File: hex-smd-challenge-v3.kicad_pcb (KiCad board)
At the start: 2 copper layers, 44 x 50 mm, 29 parts, among them CON1 AVR-ISP-6, IC1 IC1, P0 CONN_01X01, P1 CONN_01X01, P2 CONN_01X01, P3 CONN_01X01, P4 CONN_01X01

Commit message: add new version of design including v2 which went to fab
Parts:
- CON1: moved to B.Cu
- moved CON1 0.32 mm to (222.8, 86.2)
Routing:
- net Net-(CON1-Pad5): track 0.00 -> 42.3 mm, vias 0 -> 1
- net Net-(CON1-Pad4): track 24.6 -> 41.6 mm, vias 0 -> 1
- net Net-(CON1-Pad1): track 15.1 -> 28.1 mm, vias 0 -> 1
- net +BATT: track 12.0 -> 24.7 mm, vias 2 -> 3
- net Net-(CON1-Pad3): track 27.0 -> 37.0 mm, vias 0 -> 1
- net GND: track 26.7 -> 16.9 mm, vias 2 -> 4
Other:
- board text added: "OSHPark.com/ SMDChallenge"
- board text removed: "OSHPark.com/SMDChallenge"

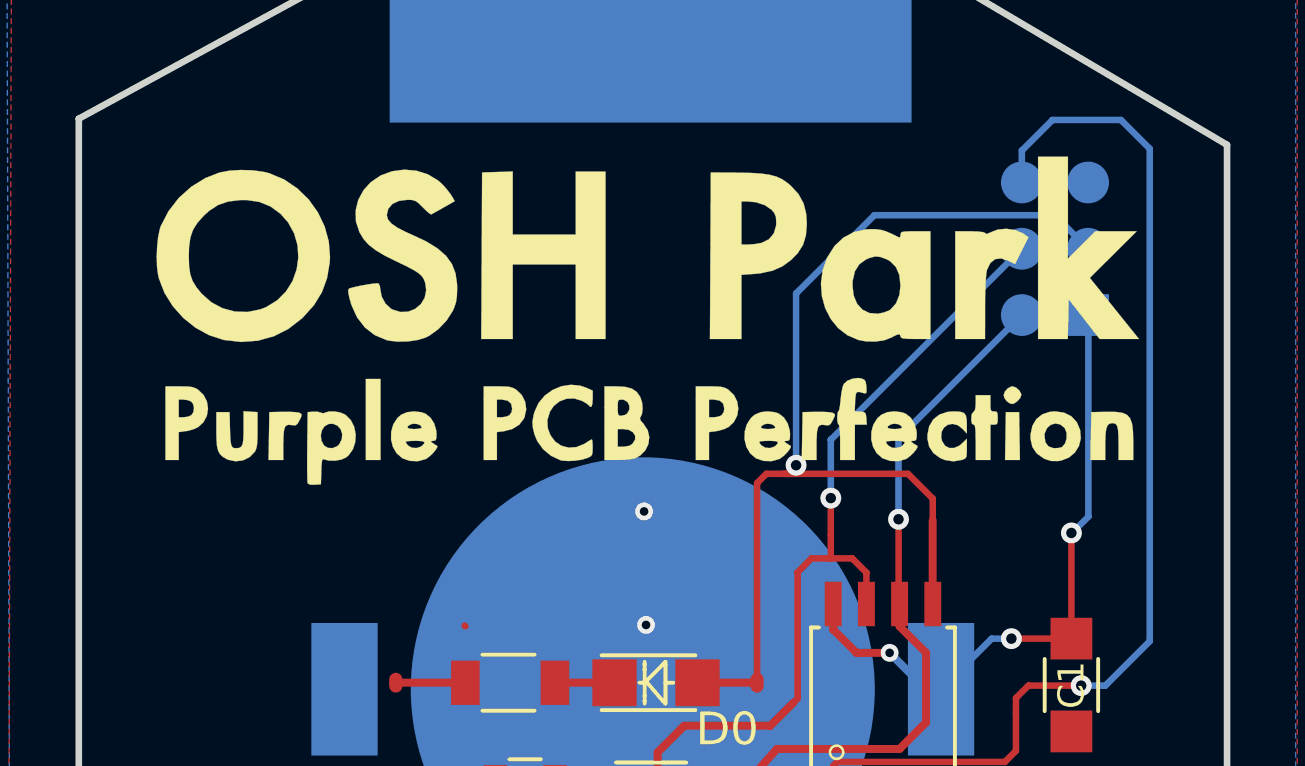
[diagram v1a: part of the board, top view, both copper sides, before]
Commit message: update logo based on svg
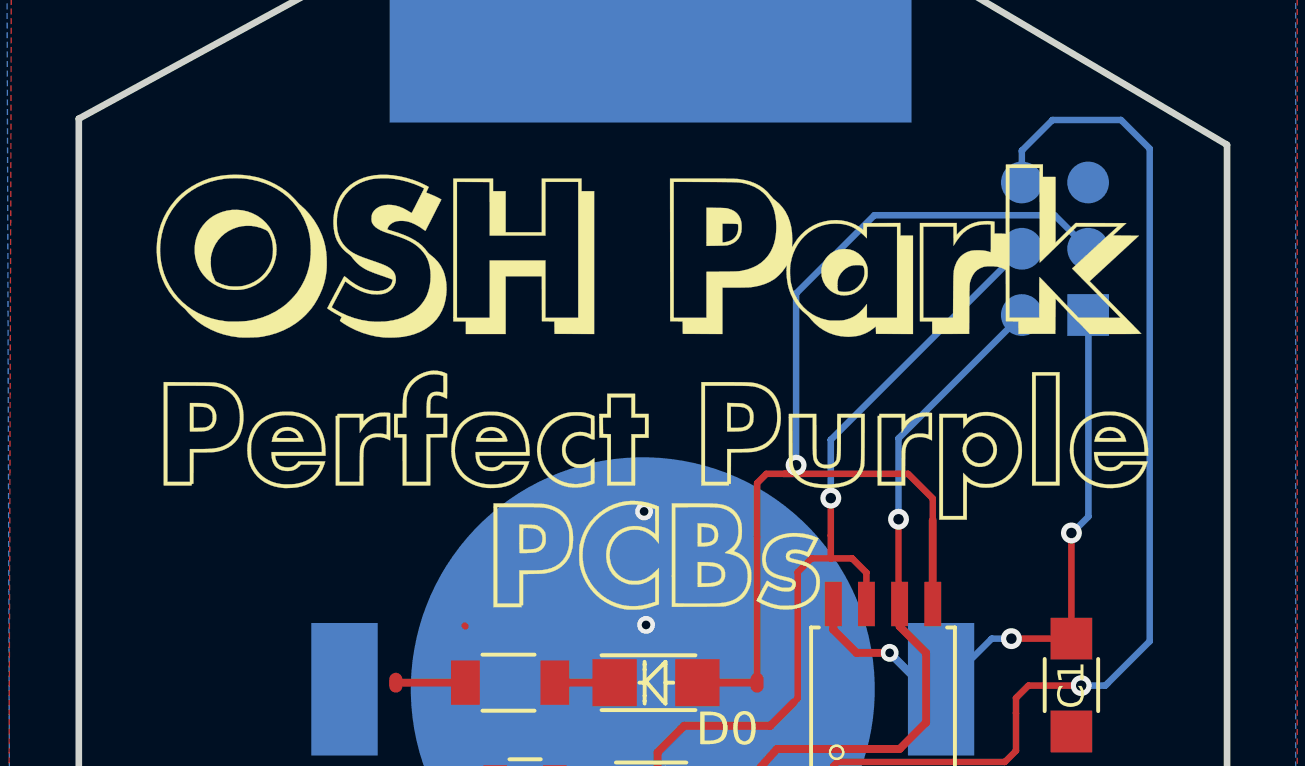
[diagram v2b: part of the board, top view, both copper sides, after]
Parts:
- removed G***: LOGO, myFootPrints:OSHParkPurple
- removed G***: LOGO, myFootPrints:OSHPark
- added Ref**: Val**, hex-smd-challenge:oshpark-v2-ppp, F.Cu at (212.9, 106.0)
- added Ref**: Val**, hex-smd-challenge:oshpark-v2-oshpark, F.Cu at (212.5, 107.1)

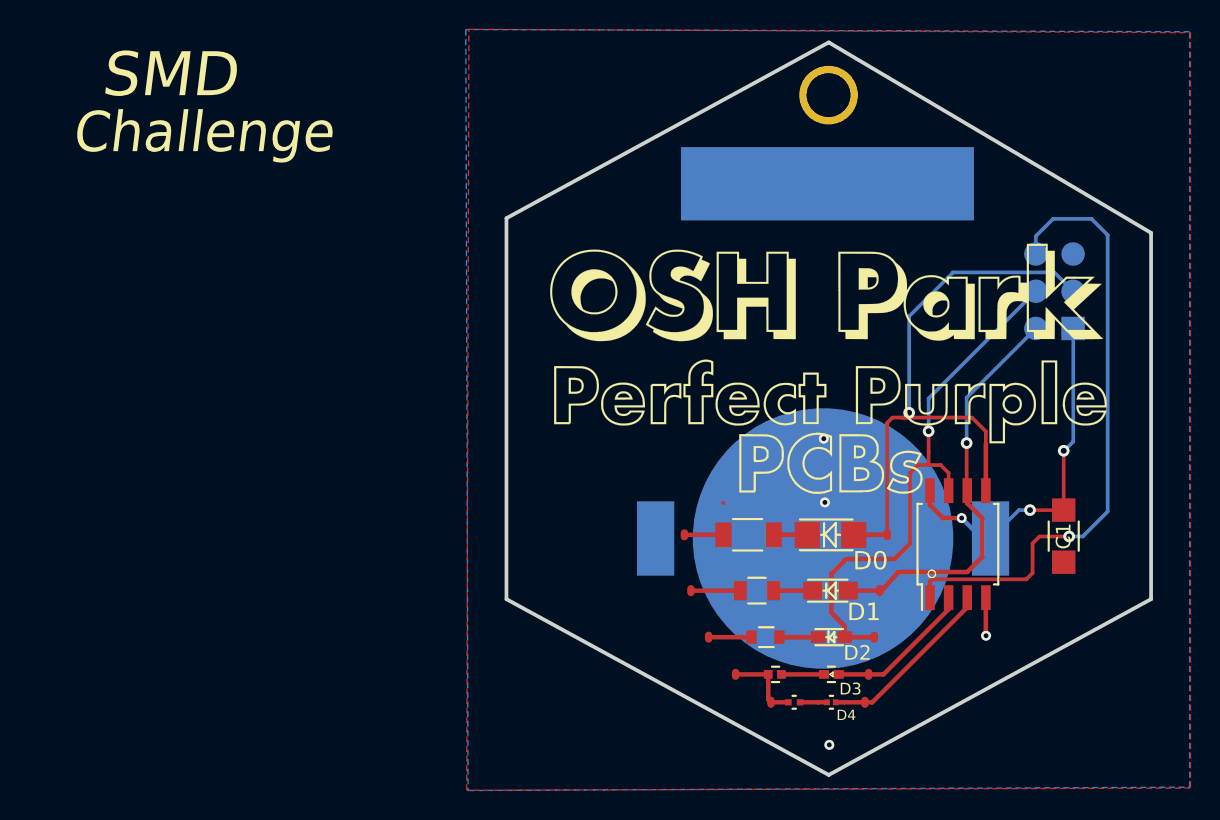
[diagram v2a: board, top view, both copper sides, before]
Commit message: improve oshpark text
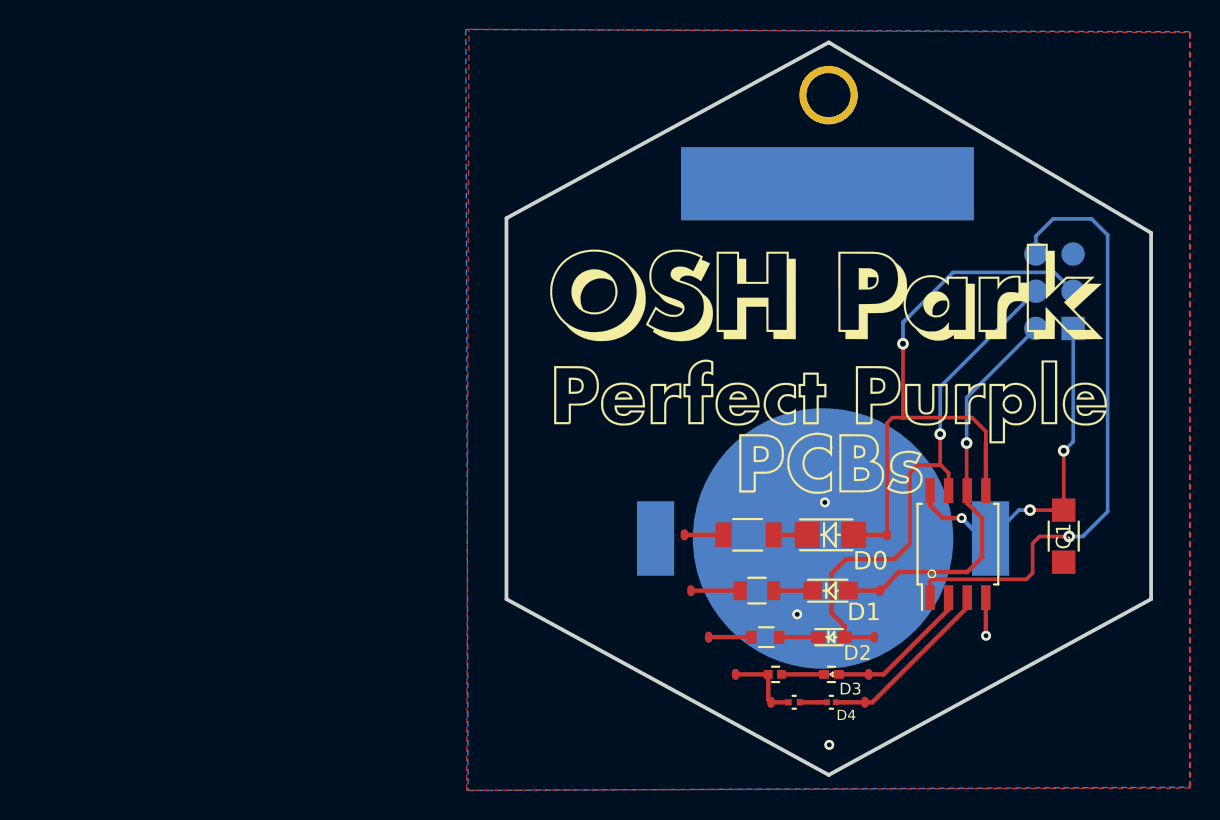
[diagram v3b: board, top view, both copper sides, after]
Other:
- board text removed: "Challenge"
- board text removed: "SMD"
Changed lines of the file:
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@@
     (effects (font (size 1 1) (thickness 0.15)) (justify left mirror))
-  )
-  (gr_text "SMD" (at 163.609 68.863) (layer "F.SilkS")
-    (effects (font (size 3 3) (thickness 0.75) italic))
-  )
-  (gr_text "Challenge" (at 165.895 72.8) (layer "F.SilkS")
-    (effects (font (size 2.75 2.6) (thickness 0.65) italic))
   )
   (segment (start 204.687 111.6925) (end 205.8745 111.6925) (width 0.3048) (layer "F.Cu") (net 1))
@@
   (segment (start 204.5045 109.7875) (end 204.5045 111.51) (width 0.3048) (layer "F.Cu") (net 1))
   (segment (start 202.274 109.7875) (end 204.5045 109.7875) (width 0.3048) (layer "F.Cu") (net 1))
-  (segment (start 201.4485 98.1035) (end 201.42 98.075) (width 0.25) (layer "F.Cu") (net 1))
   (segment (start 219.3555 107.1355) (end 219.37 107.15) (width 0.3048) (layer "F.Cu") (net 1))
   (segment (start 204.5045 111.51) (end 204.687 111.6925) (width 0.3048) (layer "F.Cu") (net 1))
   (segment (start 201.4485 100.2625) (end 198.7815 100.2625) (width 0.3048) (layer "F.Cu") (net 1))
   (segment (start 219.3555 104.5475) (end 219.3555 107.1355) (width 0.3048) (layer "F.Cu") (net 1))
-  (via (at 208.295 93.7) (size 0.6858) (drill 0.3302) (layers "F.Cu" "B.Cu") (net 1))
+  (via (at 206.48 105.69) (size 0.6858) (drill 0.3302) (layers "F.Cu" "B.Cu") (net 1))
   (via (at 208.67 114.6) (size 0.6858) (drill 0.3302) (layers "F.Cu" "B.Cu") (net 1))
   (via (at 219.37 107.15) (size 0.6858) (drill 0.3302) (layers "F.Cu" "B.Cu") (net 1))
@@
   (segment (start 222.77 86.175) (end 218.045 90.9) (width 0.25) (layer "B.Cu") (net 3))
   (segment (start 214.0215 101.0245) (end 213.1325 101.9135) (width 0.3048) (layer "F.Cu") (net 4))
+  (segment (start 216.24 93.39) (end 216.24 95.47) (width 0.25) (layer "F.Cu") (net 4))
+  (segment (start 216.24 95.47) (end 216.27 95.5) (width 0.25) (layer "F.Cu") (net 4))
   (segment (start 208.8145 102.9295) (end 209.7035 102.0405) (width 0.3048) (layer "F.Cu") (net 4))
   (segment (start 215.45 95.5) (end 216.27 95.5) (width 0.25) (layer "F.Cu") (net 4))
@@
   (segment (start 213.1325 101.9135) (end 209.8305 101.9135) (width 0.3048) (layer "F.Cu") (net 4))
   (segment (start 214.18 100.866) (end 214.18 96.03) (width 0.25) (layer "F.Cu") (net 4))
-  (segment (start 215.45 95.5) (end 215.45 94.62) (width 0.25) (layer "F.Cu") (net 4))
   (segment (start 214.0215 101.0245) (end 214.18 100.866) (width 0.25) (layer "F.Cu") (net 4))
   (segment (start 209.7035 106.4855) (end 208.8145 105.5965) (width 0.3048) (layer "F.Cu") (net 4))
   (segment (start 209.8305 101.9135) (end 209.7035 102.0405) (width 0.3048) (layer "F.Cu") (net 4))
-  (segment (start 215.45 94.62) (end 215.45 93.19) (width 0.25) (layer "F.Cu") (net 4))
   (segment (start 214.18 96.03) (end 214.71 95.5) (width 0.25) (layer "F.Cu") (net 4))
   (segment (start 208.8145 105.5965) (end 208.8145 102.9295) (width 0.3048) (layer "F.Cu") (net 4))
   (segment (start 216.27 95.5) (end 216.8155 96.0455) (width 0.25) (layer "F.Cu") (net 4))
   (segment (start 209.7035 107.2475) (end 211.7355 107.2475) (width 0.3048) (layer "F.Cu") (net 4))
-  (via (at 215.45 93.19) (size 0.8) (drill 0.4) (layers "F.Cu" "B.Cu") (net 4))
-  (segment (start 215.45 90.955) (end 215.45 93.19) (width 0.25) (layer "B.Cu") (net 4))
-  (segment (start 222.77 83.635) (end 215.4525 90.9525) (width 0.25) (layer "B.Cu") (net 4))
-  (segment (start 215.4525 90.9525) (end 215.45 90.955) (width 0.25) (layer "B.Cu") (net 4))
+  (via (at 216.24 93.39) (size 0.8) (drill 0.4) (layers "F.Cu" "B.Cu") (net 4))
+  (segment (start 222.77 83.635) (end 216.24 90.165) (width 0.25) (layer "B.Cu") (net 4))
+  (segment (start 216.24 90.165) (end 216.24 93.2) (width 0.25) (layer "B.Cu") (net 4))
+  (segment (start 216.24 93.2) (end 216.24 93.39) (width 0.25) (layer "B.Cu") (net 4))
+  (segment (start 213.7 92.26) (end 213.64 92.26) (width 0.25) (layer "F.Cu") (net 5))
   (segment (start 212.98 92.26) (end 214.04 92.26) (width 0.25) (layer "F.Cu") (net 5))
   (segment (start 219.3555 93.2055) (end 218.41 92.26) (width 0.25) (layer "F.Cu") (net 5))
   (segment (start 219.3555 97.2475) (end 219.3555 94.0395) (width 0.3048) (layer "F.Cu") (net 5))
+  (segment (start 213.7 87.22) (end 213.7 87.74) (width 0.25) (layer "F.Cu") (net 5))
+  (segment (start 214.19 92.26) (end 213.7 92.26) (width 0.25) (layer "F.Cu") (net 5))
   (segment (start 212.6245 94.6745) (end 212.6245 92.6155) (width 0.25) (layer "F.Cu") (net 5))
   (segment (start 212.6245 92.6155) (end 212.98 92.26) (width 0.25) (layer "F.Cu") (net 5))
   (segment (start 210.3385 100.2625) (end 212.6245 100.2625) (width 0.3048) (layer "F.Cu") (net 5))
-  (segment (start 214.12 91.93) (end 214.12 92.19) (width 0.25) (layer "F.Cu") (net 5))
   (segment (start 219.3555 94.0395) (end 219.3555 93.2055) (width 0.25) (layer "F.Cu") (net 5))
-  (segment (start 214.19 92.26) (end 213.64 92.26) (width 0.25) (layer "F.Cu") (net 5))
-  (segment (start 214.12 92.19) (end 214.19 92.26) (width 0.25) (layer "F.Cu") (net 5))
   (segment (start 218.41 92.26) (end 214.19 92.26) (width 0.25) (layer "F.Cu") (net 5))
   (segment (start 212.6245 100.2625) (end 212.6245 94.6745) (width 0.254) (layer "F.Cu") (net 5))
-  (via (at 214.12 91.93) (size 0.8) (drill 0.4) (layers "F.Cu" "B.Cu") (net 5))
+  (segment (start 213.7 87.74) (end 213.7 92.26) (width 0.25) (layer "F.Cu") (net 5))
+  (via (at 213.7 87.22) (size 0.8) (drill 0.4) (layers "F.Cu" "B.Cu") (net 5))
+  (segment (start 213.7 85.77) (end 213.7 87.22) (width 0.25) (layer "B.Cu") (net 5))
+  (segment (start 214.12 85.35) (end 213.84 85.63) (width 0.25) (layer "B.Cu") (net 5))
   (segment (start 225.31 83.635) (end 224.025 82.35) (width 0.25) (layer "B.Cu") (net 5))
-  (segment (start 214.12 85.35) (end 214.12 91.97) (width 0.25) (layer "B.Cu") (net 5))
   (segment (start 224.025 82.35) (end 217.12 82.35) (width 0.25) (layer "B.Cu") (net 5))
   (segment (start 217.12 82.35) (end 214.12 85.35) (width 0.25) (layer "B.Cu") (net 5))
-  (segment (start 214.12 91.97) (end 214.11 91.98) (width 0.25) (layer "B.Cu") (net 5))
+  (segment (start 213.84 85.63) (end 213.7 85.77) (width 0.25) (layer "B.Cu") (net 5))
   (segment (start 222.12 103.3) (end 215.695 103.3) (width 0.25) (layer "F.Cu") (net 6))
   (segment (start 222.545 101.425) (end 222.545 102.875) (width 0.25) (layer "F.Cu") (net 6))

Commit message: add missing silk
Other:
- board text added: "0201"
- board text added: "0402"
- board text added: "0603"
- board text added: "0805"
- board text added: "1206"
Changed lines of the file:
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@@
-(kicad_pcb (version 20201115) (generator pcbnew)
+(kicad_pcb (version 20201220) (generator pcbnew)
   (general
     (thickness 1.6)
@@
     (effects (font (size 1 1) (thickness 0.15)) (justify left mirror))
   )
+  (gr_text "0201" (at 204.3557 111.7981) (layer "F.SilkS")
+    (effects (font (size 0.762 0.762) (thickness 0.15)))
+  )
+  (gr_text "0805" (at 198.7042 104.1146) (layer "F.SilkS")
+    (effects (font (size 1.2 1.2) (thickness 0.3)))
+  )
+  (gr_text "0603" (at 199.9742 107.2896) (layer "F.SilkS")
+    (effects (font (size 1 1) (thickness 0.25)))
+  )
+  (gr_text "1206" (at 198.0692 100.3046) (layer "F.SilkS")
+    (effects (font (size 1.5 1.5) (thickness 0.3)))
+  )
+  (gr_text "0402" (at 201.8792 109.8296) (layer "F.SilkS")
+    (effects (font (size 0.889 0.889) (thickness 0.2)))
+  )
   (segment (start 204.687 111.6925) (end 205.8745 111.6925) (width 0.3048) (layer "F.Cu") (net 1))
